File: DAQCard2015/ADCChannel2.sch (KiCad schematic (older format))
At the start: 50 parts, among them U1 LTC6403, U2 AD9219, U3 LTC6403, U4 LTC6403, U5 LTC6403

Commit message: Updates to DAQ Card including FPGA card pinout and completion of ADC Stage
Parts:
- removed C1, C11, C15, C16: .01uF, symbol C
- removed C10, C2, C3, C7, C9: .1uF, symbol C
- removed C12, C13, C14, C17, C18, C19, C20, C21, C22, C4, C5, C6: C, symbol C
- removed C8: 2.2uF, symbol CP
- removed R1, R13, R14, R8: Rt, symbol R
- removed R10, R15, R16, R17, R18, R2, R3, R9: Ri, symbol R
- removed R11, R12, R19, R20, R21, R22, R5, R6: Rf, symbol R
- removed R23: 2.7k, symbol R
- removed R24: 1k, symbol R
- removed R7: 10k, symbol R
- removed U1, U3, U4, U5: LTC6403, symbol LTC6403
- removed U2: AD9219, symbol AD9219
- added C23, C33, C37, C38: .01uF, symbol C
- added C24, C25, C29, C31, C32: .1uF, symbol C
- added C26, C27, C28, C34, C35, C36, C39, C40, C41, C42, C43, C44: C, symbol C
- added C30: 2.2uF, symbol CP
- added R25, R32, R37, R38: Rt, symbol R
- added R26, R27, R33, R34, R39, R40, R41, R42: Ri, symbol R
- added R29, R30, R35, R36, R43, R44, R45, R46: Rf, symbol R
- added R31: 10k, symbol R
- added R47: 2.7k, symbol R
- added R48: 1k, symbol R
- added U10, U6, U8, U9: LTC6403, symbol LTC6403
- added U7: AD9219, symbol AD9219
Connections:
- net labels added: 18ana
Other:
- note added: "100R Termination \nis common for all ADCs."

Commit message: Adds power circuitry to DAQCard2015
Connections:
- net labels removed: 18ana
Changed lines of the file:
@@
 GNDana
 Text GLabel 1300 3350 0    60   Input ~ 0
-18ana
+1V8ana
 Text GLabel 1300 3500 0    60   Input ~ 0
 3V3

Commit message: Replaces single ample with 4-channel varients. Greatly reducing part count
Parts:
- removed C23, C33, C37, C38: .01uF, symbol C
- removed C24, C25, C29, C31, C32: .1uF, symbol C
- removed C26, C27, C28, C34, C35, C36, C39, C40, C41, C42, C43, C44: C, symbol C
- removed C30: 2.2uF, symbol CP
- removed R25, R32, R37, R38: Rt, symbol R
- removed R26, R27, R33, R34, R39, R40, R41, R42: Ri, symbol R
- removed R29, R30, R35, R36, R43, R44, R45, R46: Rf, symbol R
- removed R31: 10k, symbol R
- removed R47: 2.7k, symbol R
- removed R48: 1k, symbol R
- removed U10, U6, U8, U9: LTC6403, symbol LTC6403
- removed U7: AD9219, symbol AD9219
- added C12, C13, C14: C, symbol C
- added C15: .01uF, symbol C
- added C16, C17, C18, C20, C21: .1uF, symbol C
- added C19: 2.2uF, symbol CP
- added R11, R12, R13, R14: Rt, symbol R
- added R15: 2.7k, symbol R
- added R16: 1k, symbol R
- added R17: 10k, symbol R
- added RP4: R_PACK8, symbol R_PACK8
- added RP5, RP6: Rf, symbol R_PACK4
- added U4: THS4524IDBTR, symbol THS4524IDBTR
- added U5: AD9219, symbol AD9219
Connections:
- net labels added: 3V3ana, VOCM
- net labels removed: 3V3, Vocm
- wire segments 178 -> 192
- no-connect marks 12 -> 4
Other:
- note removed: "100R Termination \nis common for all ADCs."

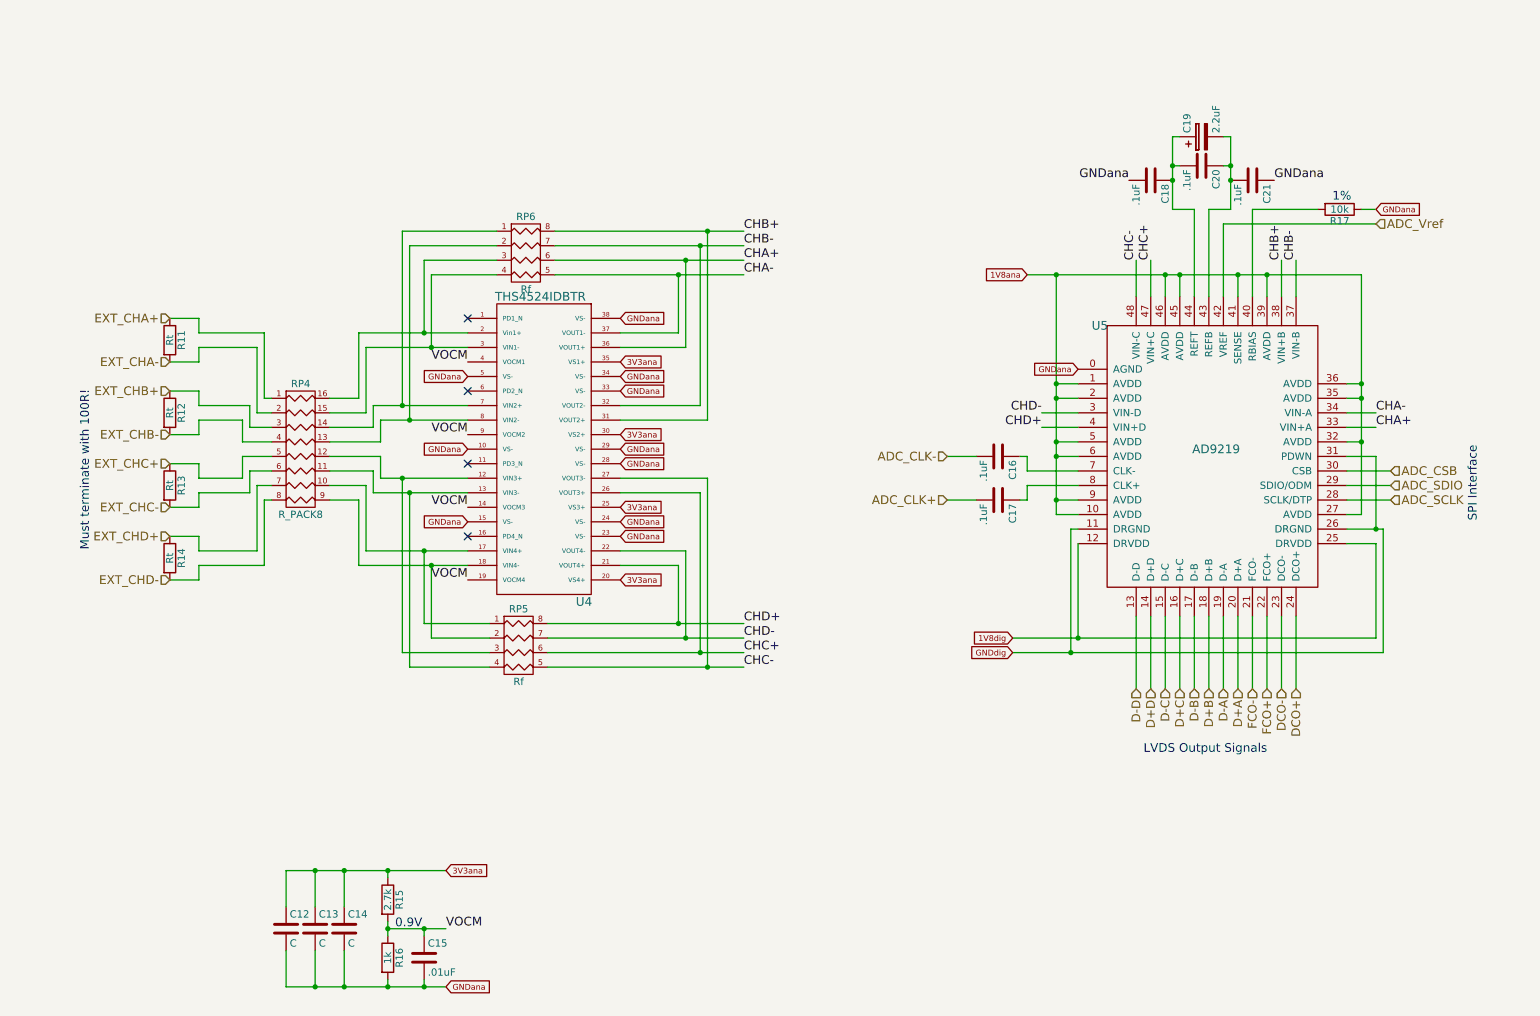
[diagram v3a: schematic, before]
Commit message: Finishes initial version of schematic(mostly). And adds a whole bunch of new footprints!
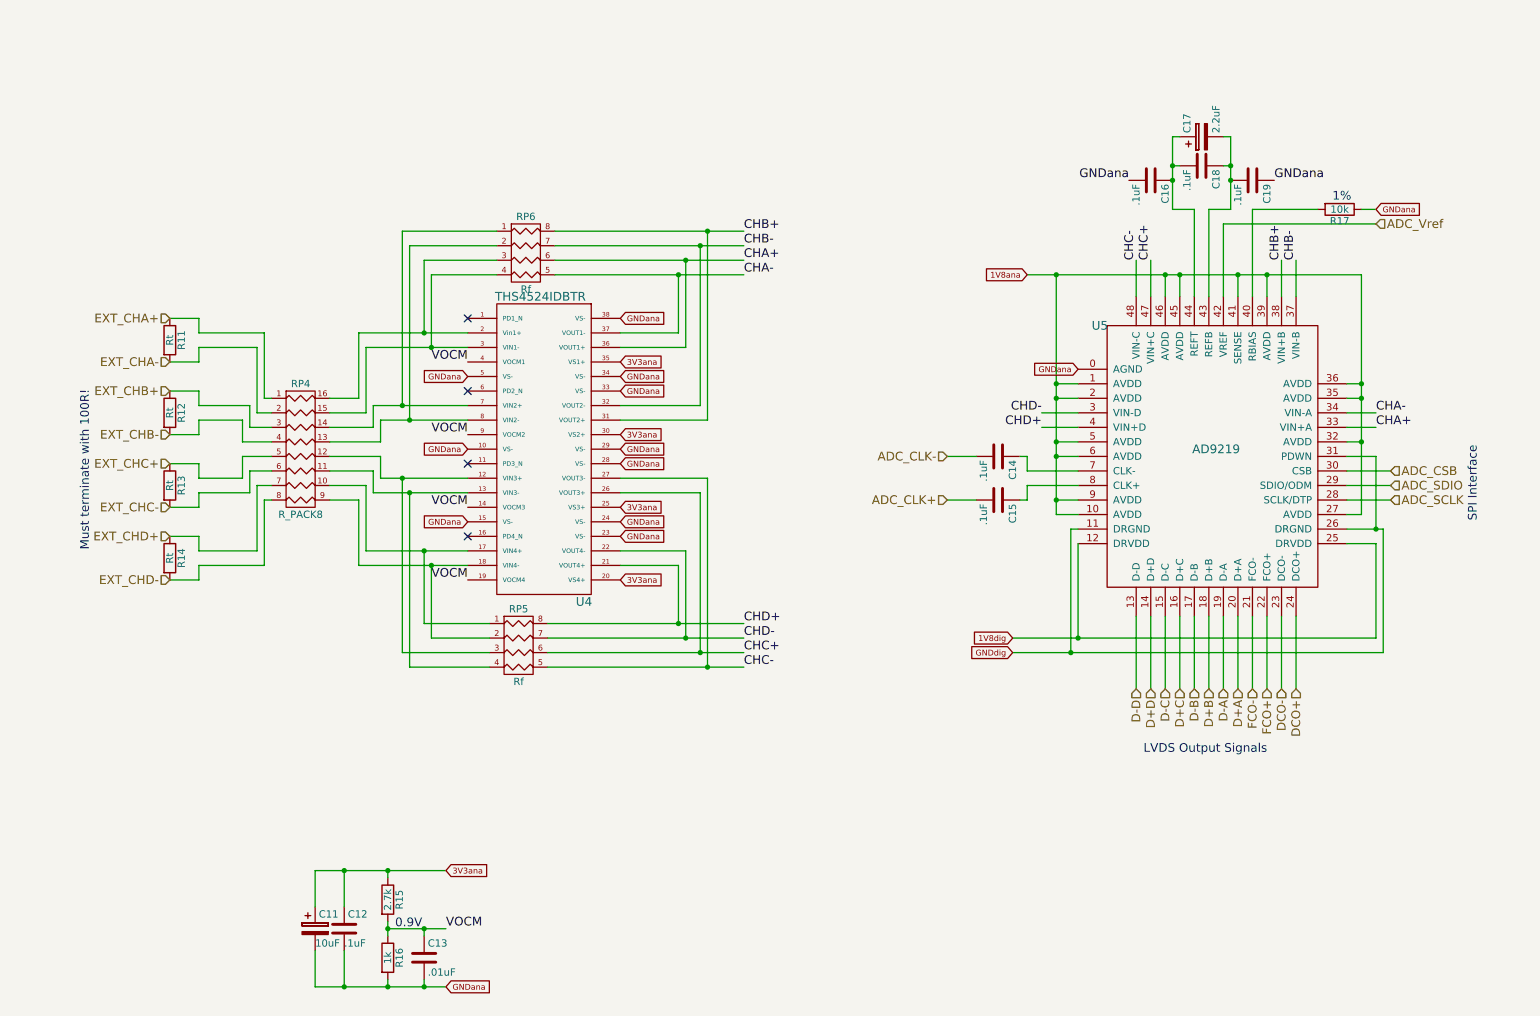
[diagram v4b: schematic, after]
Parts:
- removed C17, C20, C21: .1uF, symbol C
- removed C19: 2.2uF, symbol CP
- added C11: 10uF, extras:SMD_Cap_3mmDia, symbol CP
- added C17: 2.2uF, extras:SMD_Cap_3mmDia, symbol CP
- added C19: .1uF, Capacitors_SMD:C_0603, symbol C
- C12, C14: value C -> .1uF; footprint (none) -> Capacitors_SMD:C_0603
- C13: value C -> .01uF; footprint (none) -> Capacitors_SMD:C_0603
- C15: value .01uF -> .1uF; footprint (none) -> Capacitors_SMD:C_0603
- C16, C18: footprint (none) -> Capacitors_SMD:C_0603
- R11, R12, R13, R14, R15, R16, R17: footprint (none) -> Resistors_SMD:R_0603
- RP4: footprint (none) -> extras:R8_MNR18
- RP5, RP6: footprint (none) -> extras:R4-MNR04
- U4: footprint (none) -> Housings_SSOP:TSSOP-38_4.4x9.7mm_Pitch0.5mm
- U5: footprint (none) -> SMD_Packages:QFN-48-1EP
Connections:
- net 3V3ana: now also C11.1; no longer C13.1, C14.1
- net ADC_CLK+: now also C15.2
- net ADC_CLK-: now also C14.2; no longer C16.2
- net GNDana: now also C16.2, C11.2, C19.1; no longer C14.2, C15.2, C18.2
- net VOCM: now also C13.1; no longer C15.1
- net at U5.43 (REFB): now also C18.1, C17.2, C19.2
- net at U5.44 (REFT): now also C16.1, C18.2, C17.1; no longer C18.1
- net at U5.7 (CLK-): now also C14.1; no longer C16.1
- net at U5.8 (CLK+): now also C15.1
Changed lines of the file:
@@
 $Comp
 L AD9219 U5
-U 1 1 55CFF5AB
+U 1 1 55CB5757
 P 9050 3700
 F 0 "U5" H 8250 4650 60  0000 C CNN
 F 1 "AD9219" H 9050 3800 60  0000 C CNN
-F 2 "" H 8650 3700 60  0000 C CNN
+F 2 "SMD_Packages:QFN-48-1EP" H 8650 3700 60  0001 C CNN
 F 3 "" H 8650 3700 60  0000 C CNN
 	1    9050 3700
@@
 $Comp
 L R R15
-U 1 1 55CFF5F6
+U 1 1 55CB578A
 P 3350 6700
 F 0 "R15" V 3430 6700 50  0000 C CNN
 F 1 "2.7k" V 3350 6700 50  0000 C CNN
-F 2 "" V 3280 6700 30  0000 C CNN
+F 2 "Resistors_SMD:R_0603" V 3280 6700 30  0001 C CNN
 F 3 "" H 3350 6700 30  0000 C CNN
 	1    3350 6700
@@
 $Comp
 L R R16
-U 1 1 55CFF5E2
+U 1 1 55CB5776
 P 3350 7100
 F 0 "R16" V 3430 7100 50  0000 C CNN
 F 1 "1k" V 3350 7100 50  0000 C CNN
-F 2 "" V 3280 7100 30  0000 C CNN
+F 2 "Resistors_SMD:R_0603" V 3280 7100 30  0001 C CNN
 F 3 "" H 3350 7100 30  0000 C CNN
 	1    3350 7100
@@
 $Comp
 L C C12
-U 1 1 55CFF5CA
-P 2650 6900
-F 0 "C12" H 2675 7000 50  0000 L CNN
-F 1 "C" H 2675 6800 50  0000 L CNN
-F 2 "" H 2688 6750 30  0000 C CNN
-F 3 "" H 2650 6900 60  0000 C CNN
-	1    2650 6900
-	1    0    0    -1
-$EndComp
-$Comp
-L C C13
-U 1 1 55CFF5B3
-P 2850 6900
-F 0 "C13" H 2875 7000 50  0000 L CNN
-F 1 "C" H 2875 6800 50  0000 L CNN
-F 2 "" H 2888 6750 30  0000 C CNN
-F 3 "" H 2850 6900 60  0000 C CNN
-	1    2850 6900
-	1    0    0    -1
-$EndComp
-$Comp
-L C C14
-U 1 1 55CFF5BA
+U 1 1 55CFF5BB
 P 3050 6900
-F 0 "C14" H 3075 7000 50  0000 L CNN
-F 1 "C" H 3075 6800 50  0000 L CNN
-F 2 "" H 3088 6750 30  0000 C CNN
+F 0 "C12" H 3075 7000 50  0000 L CNN
+F 1 ".1uF" H 3050 6800 50  0000 L CNN
+F 2 "Capacitors_SMD:C_0603" H 3088 6750 30  0001 C CNN
 F 3 "" H 3050 6900 60  0000 C CNN
 	1    3050 6900
@@
 ADC_SCLK
 $Comp
-L C C16
-U 1 1 55CFF5C3
+L C C14
+U 1 1 55CB5764
 P 7550 3650
-F 0 "C16" H 7575 3750 50  0000 L CNN
+F 0 "C14" H 7575 3750 50  0000 L CNN
 F 1 ".1uF" H 7575 3550 50  0000 L CNN
-F 2 "" H 7588 3500 30  0000 C CNN
+F 2 "Capacitors_SMD:C_0603" H 7588 3500 30  0001 C CNN
 F 3 "" H 7550 3650 60  0000 C CNN
 	1    7550 3650
@@
 $EndComp
 $Comp
-L C C17
-U 1 1 55CFF5E7
+L C C15
+U 1 1 55CB5749
 P 7550 3950
-F 0 "C17" H 7575 4050 50  0000 L CNN
+F 0 "C15" H 7575 4050 50  0000 L CNN
 F 1 ".1uF" H 7575 3850 50  0000 L CNN
-F 2 "" H 7588 3800 30  0000 C CNN
+F 2 "Capacitors_SMD:C_0603" H 7588 3800 30  0001 C CNN
 F 3 "" H 7550 3950 60  0000 C CNN
 	1    7550 3950
@@
 DCO+
 $Comp
-L C C21
-U 1 1 55CFF5FD
+L C C19
+U 1 1 55CB5790
 P 9300 1750
-F 0 "C21" H 9325 1850 50  0000 L CNN
+F 0 "C19" H 9325 1850 50  0000 L CNN
 F 1 ".1uF" H 9325 1650 50  0000 L CNN
-F 2 "" H 9338 1600 30  0000 C CNN
+F 2 "Capacitors_SMD:C_0603" H 9338 1600 30  0001 C CNN
 F 3 "" H 9300 1750 60  0000 C CNN
 	1    9300 1750
@@
 $EndComp
 $Comp
-L C C18
-U 1 1 55CFF5D3
+L C C16
+U 1 1 55CB576B
 P 8600 1750
-F 0 "C18" H 8625 1850 50  0000 L CNN
+F 0 "C16" H 8625 1850 50  0000 L CNN
 F 1 ".1uF" H 8625 1650 50  0000 L CNN
-F 2 "" H 8638 1600 30  0000 C CNN
+F 2 "Capacitors_SMD:C_0603" H 8638 1600 30  0001 C CNN
 F 3 "" H 8600 1750 60  0000 C CNN
 	1    8600 1750
@@
 $EndComp
 $Comp
-L C C20
-U 1 1 55C98FC1
+L C C18
+U 1 1 55CB5771
 P 8950 1650
-F 0 "C20" H 8975 1750 50  0000 L CNN
+F 0 "C18" H 8975 1750 50  0000 L CNN
 F 1 ".1uF" H 8975 1550 50  0000 L CNN
-F 2 "" H 8988 1500 30  0000 C CNN
+F 2 "Capacitors_SMD:C_0603" H 8988 1500 30  0001 C CNN
 F 3 "" H 8950 1650 60  0000 C CNN
 	1    8950 1650
@@
 GNDana
 $Comp
-L CP C19
-U 1 1 55CFF602
+L CP C17
+U 1 1 55CB5798
 P 8950 1450
-F 0 "C19" H 8975 1550 50  0000 L CNN
+F 0 "C17" H 8975 1550 50  0000 L CNN
 F 1 "2.2uF" H 8975 1350 50  0000 L CNN
-F 2 "" H 8988 1300 30  0000 C CNN
+F 2 "extras:SMD_Cap_3mmDia" H 8988 1300 30  0001 C CNN
 F 3 "" H 8950 1450 60  0000 C CNN
 	1    8950 1450
@@
 $Comp
 L R R17
-U 1 1 55CFF5EB
+U 1 1 55CB5781
 P 9900 1950
 F 0 "R17" V 9980 1950 50  0000 C CNN
 F 1 "10k" V 9900 1950 50  0000 C CNN
-F 2 "" V 9830 1950 30  0000 C CNN
+F 2 "Resistors_SMD:R_0603" V 9830 1950 30  0001 C CNN
 F 3 "" H 9900 1950 30  0000 C CNN
 	1    9900 1950
@@
 $Comp
 L THS4524IDBTR U4
-U 1 1 55CE58EE
+U 1 1 55CB5799
 P 4400 3700
 F 0 "U4" H 4700 2750 60  0000 C CNN
 F 1 "THS4524IDBTR" H 4400 4850 60  0000 C CNN
-F 2 "" H 4600 3800 60  0000 C CNN
+F 2 "Housings_SSOP:TSSOP-38_4.4x9.7mm_Pitch0.5mm" H 4600 3800 60  0001 C CNN
 F 3 "" H 4600 3800 60  0000 C CNN
 	1    4400 3700
@@
 $EndComp
 $Comp
-L C C15
-U 1 1 55CFF60E
+L C C13
+U 1 1 55CB57A3
 P 3600 7100
-F 0 "C15" H 3625 7200 50  0000 L CNN
+F 0 "C13" H 3625 7200 50  0000 L CNN
 F 1 ".01uF" H 3625 7000 50  0000 L CNN
-F 2 "" H 3638 6950 30  0000 C CNN
+F 2 "Capacitors_SMD:C_0603" H 3638 6950 30  0001 C CNN
 F 3 "" H 3600 7100 60  0000 C CNN
 	1    3600 7100
@@
 Connection ~ 3600 6900
 Wire Wire Line
-	2650 6500 3750 6500
-Wire Wire Line
 	3050 6500 3050 6750
 Connection ~ 3350 6500
@@
 Connection ~ 3050 6500
 Wire Wire Line
-	2650 6500 2650 6750
-Connection ~ 2850 6500
-Wire Wire Line
-	2650 7300 3750 7300
-Wire Wire Line
 	3050 7300 3050 7050
 Wire Wire Line
 	2850 7300 2850 7050
 Connection ~ 3050 7300
-Wire Wire Line
-	2650 7300 2650 7050
-Connection ~ 2850 7300
 Wire Wire Line
 	3600 7300 3600 7250
@@
 $Comp
 L R R14
-U 1 1 55CFF616
+U 1 1 55CB57AA
 P 1850 4350
 F 0 "R14" V 1930 4350 50  0000 C CNN
 F 1 "Rt" V 1850 4350 50  0000 C CNN
-F 2 "" V 1780 4350 30  0000 C CNN
+F 2 "Resistors_SMD:R_0603" V 1780 4350 30  0001 C CNN
 F 3 "" H 1850 4350 30  0000 C CNN
 	1    1850 4350
@@
 $Comp
 L R R13
-U 1 1 55CFF61E
+U 1 1 55CB57AE
 P 1850 3850
 F 0 "R13" V 1930 3850 50  0000 C CNN
 F 1 "Rt" V 1850 3850 50  0000 C CNN
-F 2 "" V 1780 3850 30  0000 C CNN
+F 2 "Resistors_SMD:R_0603" V 1780 3850 30  0001 C CNN
 F 3 "" H 1850 3850 30  0000 C CNN
 	1    1850 3850
@@
 $Comp
 L R R12
-U 1 1 55CFF622
+U 1 1 55CB57B9
 P 1850 3350
 F 0 "R12" V 1930 3350 50  0000 C CNN
 F 1 "Rt" V 1850 3350 50  0000 C CNN
-F 2 "" V 1780 3350 30  0000 C CNN
+F 2 "Resistors_SMD:R_0603" V 1780 3350 30  0001 C CNN
 F 3 "" H 1850 3350 30  0000 C CNN
 	1    1850 3350
@@
 $Comp
 L R R11
-U 1 1 55CFF62D
+U 1 1 55CB57BC
 P 1850 2850
 F 0 "R11" V 1930 2850 50  0000 C CNN
 F 1 "Rt" V 1850 2850 50  0000 C CNN
-F 2 "" V 1780 2850 30  0000 C CNN
+F 2 "Resistors_SMD:R_0603" V 1780 2850 30  0001 C CNN
 F 3 "" H 1850 2850 30  0000 C CNN
 	1    1850 2850
@@
 $Comp
 L R_PACK4 RP5
-U 1 1 55CFF631
+U 1 1 55CB57C3
 P 4250 5150
 F 0 "RP5" H 4250 5600 50  0000 C CNN
 F 1 "Rf" H 4250 5100 50  0000 C CNN
-F 2 "" H 4250 5150 60  0000 C CNN
+F 2 "extras:R4-MNR04" H 4250 5150 60  0001 C CNN
 F 3 "" H 4250 5150 60  0000 C CNN
 	1    4250 5150
@@
 $Comp
 L R_PACK4 RP6
-U 1 1 55CFF638
+U 1 1 55CF51DE
 P 4300 2450
 F 0 "RP6" H 4300 2900 50  0000 C CNN
 F 1 "Rf" H 4300 2400 50  0000 C CNN
-F 2 "" H 4300 2450 60  0000 C CNN
+F 2 "extras:R4-MNR04" H 4300 2450 60  0001 C CNN
 F 3 "" H 4300 2450 60  0000 C CNN
 	1    4300 2450
@@
 $Comp
 L R_PACK8 RP4
-U 1 1 55CF6A0D
+U 1 1 55CB57CB
 P 2750 3600
 F 0 "RP4" H 2750 4050 50  0000 C CNN
 F 1 "R_PACK8" H 2750 3150 50  0000 C CNN
-F 2 "" H 2750 3600 60  0000 C CNN
+F 2 "extras:R8_MNR18" H 2750 3600 60  0001 C CNN
 F 3 "" H 2750 3600 60  0000 C CNN
 	1    2750 3600
@@
 Text GLabel 10150 1950 2    40   Input ~ 0
 GNDana
+Wire Wire Line
+	3750 6500 2850 6500
+Wire Wire Line
+	2850 7300 3750 7300
+$Comp
+L CP C11
+U 1 1 55CB5744
+P 2850 6900
+F 0 "C11" H 2875 7000 50  0000 L CNN
+F 1 "10uF" H 2850 6800 50  0000 L CNN
+F 2 "extras:SMD_Cap_3mmDia" H 2888 6750 30  0001 C CNN
+F 3 "" H 2850 6900 60  0000 C CNN
+	1    2850 6900
+	1    0    0    -1
+$EndComp
 $EndSCHEMATC

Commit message: Adds a more-or-less complete BOM to DAQ Card
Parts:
- C13: value .01uF -> 10000pF
- RP4: value R_PACK8 -> Ri
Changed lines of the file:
@@
 $Descr A4 11693 8268
 encoding utf-8
-Sheet 3 13
+Sheet 4 13
 Title ""
 Date ""
@@
 P 3600 7100
 F 0 "C13" H 3625 7200 50  0000 L CNN
-F 1 ".01uF" H 3625 7000 50  0000 L CNN
+F 1 "10000pF" H 3625 7000 50  0000 L CNN
 F 2 "Capacitors_SMD:C_0603" H 3638 6950 30  0001 C CNN
 F 3 "" H 3600 7100 60  0000 C CNN
@@
 P 2750 3600
 F 0 "RP4" H 2750 4050 50  0000 C CNN
-F 1 "R_PACK8" H 2750 3150 50  0000 C CNN
+F 1 "Ri" H 2750 3150 50  0000 C CNN
 F 2 "extras:R8_MNR18" H 2750 3600 60  0001 C CNN
 F 3 "" H 2750 3600 60  0000 C CNN

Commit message: Updates to DAQCard2015, especially to power systems
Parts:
- C11, C17: footprint extras:SMD_Cap_3mmDia -> Capacitors_SMD:C_0805
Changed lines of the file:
@@
 F 0 "C17" H 8975 1550 50  0000 L CNN
 F 1 "2.2uF" H 8975 1350 50  0000 L CNN
-F 2 "extras:SMD_Cap_3mmDia" H 8988 1300 30  0001 C CNN
+F 2 "Capacitors_SMD:C_0805" H 8988 1300 30  0001 C CNN
 F 3 "" H 8950 1450 60  0000 C CNN
 	1    8950 1450
@@
 F 0 "C11" H 2875 7000 50  0000 L CNN
 F 1 "10uF" H 2850 6800 50  0000 L CNN
-F 2 "extras:SMD_Cap_3mmDia" H 2888 6750 30  0001 C CNN
+F 2 "Capacitors_SMD:C_0805" H 2888 6750 30  0001 C CNN
 F 3 "" H 2850 6900 60  0000 C CNN
 	1    2850 6900
